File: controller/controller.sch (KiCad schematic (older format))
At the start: 46 parts, among them J1 j0011d21bnl, J2 swim_header, SW1 SW_left, SW2 SW_a0, SW3 SW_right, SW4 SW_a1, SW5 SW_up, SW6 SW_back_r, SW7 SW_down, SW8 SW_back_l, U1 74HCT541, U2 STM8L101F3P

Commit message: Update footprint for controller buffer
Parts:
- U1: footprint Package_SO:TSSOP-20_4.4x6.5mm_P0.65mm -> Package_SO:SSOP-20_5.3x7.2mm_P0.65mm
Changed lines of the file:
@@
 F 0 "U1" H 6150 3950 50  0000 C CNN
 F 1 "74HCT541" H 6100 2650 50  0000 C CNN
-F 2 "Package_SO:TSSOP-20_4.4x6.5mm_P0.65mm" H 5900 3300 50  0001 C CNN
+F 2 "Package_SO:SSOP-20_5.3x7.2mm_P0.65mm" H 5900 3300 50  0001 C CNN
 F 3 "http://www.ti.com/lit/gpn/sn74HCT541" H 5900 3300 50  0001 C CNN
 	1    5900 3300

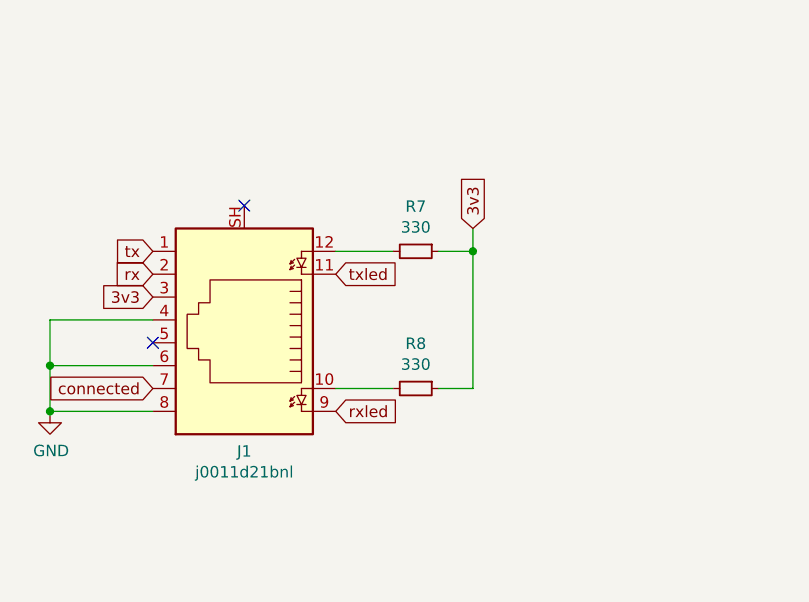
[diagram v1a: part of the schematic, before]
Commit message: Add ctrl sw
found issue with leds on rj45
might have problems with uart pins in rj45
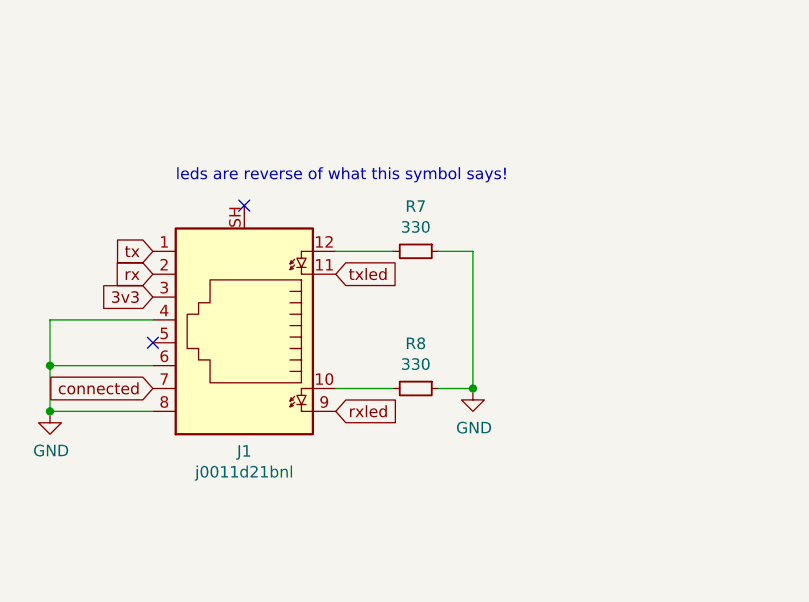
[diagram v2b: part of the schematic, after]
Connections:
- net 3v3: no longer R7.1, R8.1
- net GND: now also R7.1, R8.1
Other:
- note added: "leds are reverse of what this symbol says!"
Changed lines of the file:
@@
 Text GLabel 2650 3150 2    50   Input ~ 0
 rxled
-Text GLabel 3250 2350 1    50   Input ~ 0
-3v3
-Wire Wire Line
-	3250 2350 3250 2450
 Wire Wire Line
 	3250 3050 3100 3050
 Wire Wire Line
 	3100 2450 3250 2450
-Connection ~ 3250 2450
 Wire Wire Line
 	3250 2450 3250 3050
@@
 NoConn ~ 7250 2500
 NoConn ~ 7250 2600
+$Comp
+L power:GND #PWR?
+U 1 1 612D53B4
+P 3250 3050
+F 0 "#PWR?" H 3250 2800 50  0001 C CNN
+F 1 "GND" H 3255 2877 50  0000 C CNN
+F 2 "" H 3250 3050 50  0001 C CNN
+F 3 "" H 3250 3050 50  0001 C CNN
+	1    3250 3050
+	1    0    0    -1
+$EndComp
+Connection ~ 3250 3050
+Text Notes 1950 2150 0    50   ~ 0
+leds are reverse of what this symbol says!
 $EndSCHEMATC

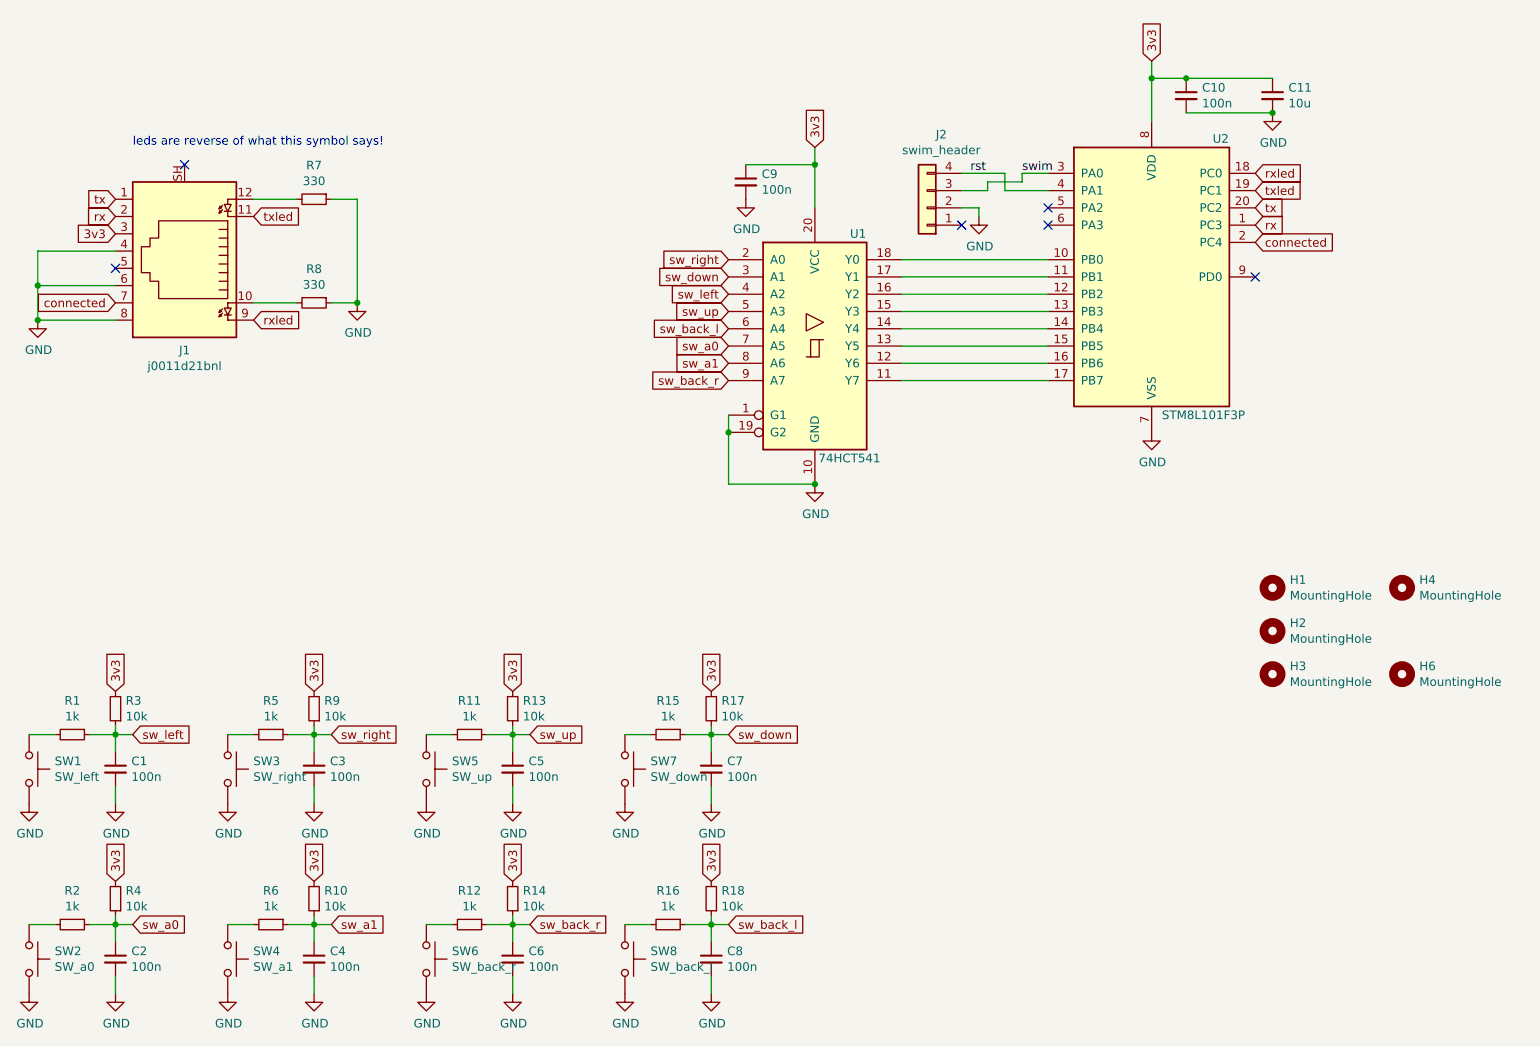
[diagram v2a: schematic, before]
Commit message: Rev 2 controller PCB
Now uses correct rj45 footprint.
Leds should work!
Added 1 more mounting hole (H5)
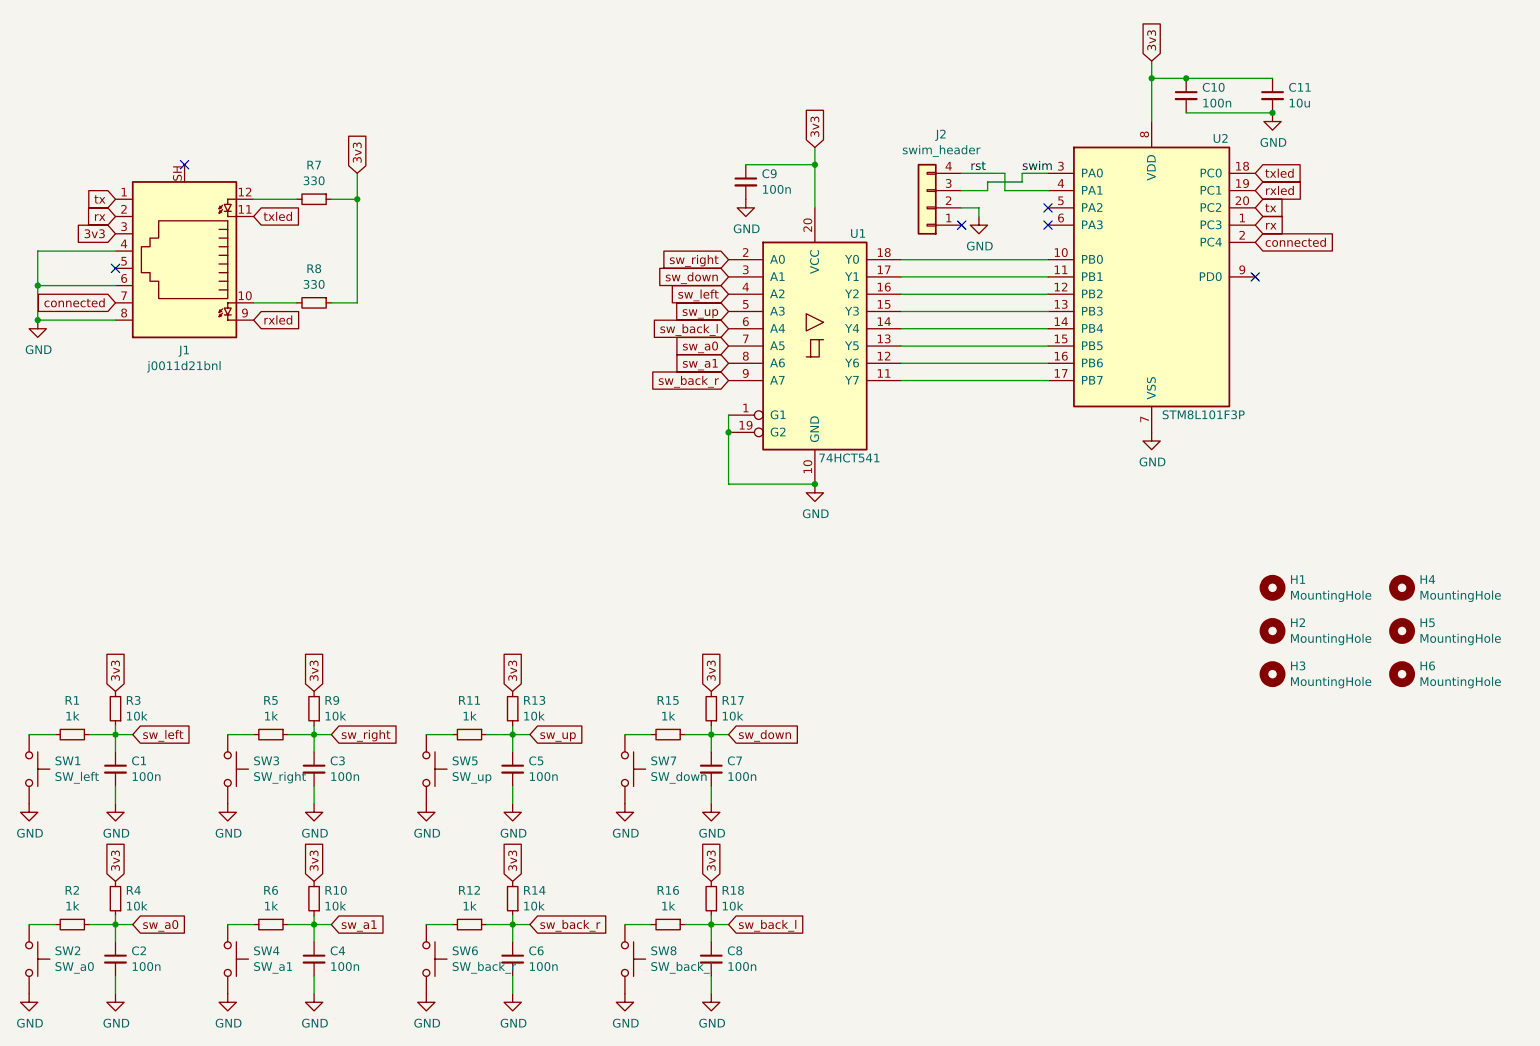
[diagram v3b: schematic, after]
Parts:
- added H5: MountingHole, MountingHole:MountingHole_3.2mm_M3, symbol Mechanical:MountingHole
- J1: footprint Connector_RJ:RJ45_Cetus_J1B1211CCD_Horizontal -> Connector_RJ:RJ45_BEL_SS74301-00x_Vertical
- U1: footprint Package_SO:SSOP-20_5.3x7.2mm_P0.65mm -> Package_SO:TSSOP-20_4.4x6.5mm_P0.65mm
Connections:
- net 3v3: now also R7.1, R8.1
- net GND: no longer R7.1, R8.1
- net rxled: now also U2.19 (PC1); no longer U2.18 (PC0)
- net txled: now also U2.18 (PC0); no longer U2.19 (PC1)
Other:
- note removed: "leds are reverse of what this symbol says!"
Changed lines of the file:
@@
 F 0 "J1" H 2250 3325 50  0000 C CNN
 F 1 "j0011d21bnl" H 2250 3416 50  0000 C CNN
-F 2 "Connector_RJ:RJ45_Cetus_J1B1211CCD_Horizontal" V 2250 2775 50  0001 C CNN
+F 2 "Connector_RJ:RJ45_BEL_SS74301-00x_Vertical" V 2250 2775 50  0001 C CNN
 F 3 "~" V 2250 2775 50  0001 C CNN
 	1    2250 2750
@@
 Text GLabel 8450 2700 2    50   Input ~ 0
 connected
+Text GLabel 8450 2400 2    50   Input ~ 0
+rxled
 Text GLabel 8450 2300 2    50   Input ~ 0
-rxled
-Text GLabel 8450 2400 2    50   Input ~ 0
 txled
 Text GLabel 2650 2550 2    50   Input ~ 0
@@
 F 0 "U1" H 6150 3950 50  0000 C CNN
 F 1 "74HCT541" H 6100 2650 50  0000 C CNN
-F 2 "Package_SO:SSOP-20_5.3x7.2mm_P0.65mm" H 5900 3300 50  0001 C CNN
+F 2 "Package_SO:TSSOP-20_4.4x6.5mm_P0.65mm" H 5900 3300 50  0001 C CNN
 F 3 "http://www.ti.com/lit/gpn/sn74HCT541" H 5900 3300 50  0001 C CNN
 	1    5900 3300
@@
 NoConn ~ 7250 2500
 NoConn ~ 7250 2600
-$Comp
-L power:GND #PWR?
-U 1 1 612D53B4
-P 3250 3050
-F 0 "#PWR?" H 3250 2800 50  0001 C CNN
-F 1 "GND" H 3255 2877 50  0000 C CNN
-F 2 "" H 3250 3050 50  0001 C CNN
-F 3 "" H 3250 3050 50  0001 C CNN
-	1    3250 3050
-	1    0    0    -1
-$EndComp
-Connection ~ 3250 3050
-Text Notes 1950 2150 0    50   ~ 0
-leds are reverse of what this symbol says!
+Text GLabel 3250 2300 1    50   Input ~ 0
+3v3
+Wire Wire Line
+	3250 2300 3250 2450
+Connection ~ 3250 2450
+$Comp
+L Mechanical:MountingHole H5
+U 1 1 613711C0
+P 9300 4950
+F 0 "H5" H 9400 4996 50  0000 L CNN
+F 1 "MountingHole" H 9400 4905 50  0000 L CNN
+F 2 "MountingHole:MountingHole_3.2mm_M3" H 9300 4950 50  0001 C CNN
+F 3 "~" H 9300 4950 50  0001 C CNN
+	1    9300 4950
+	1    0    0    -1
+$EndComp
 $EndSCHEMATC
